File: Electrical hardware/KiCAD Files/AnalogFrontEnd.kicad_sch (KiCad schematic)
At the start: 0 parts

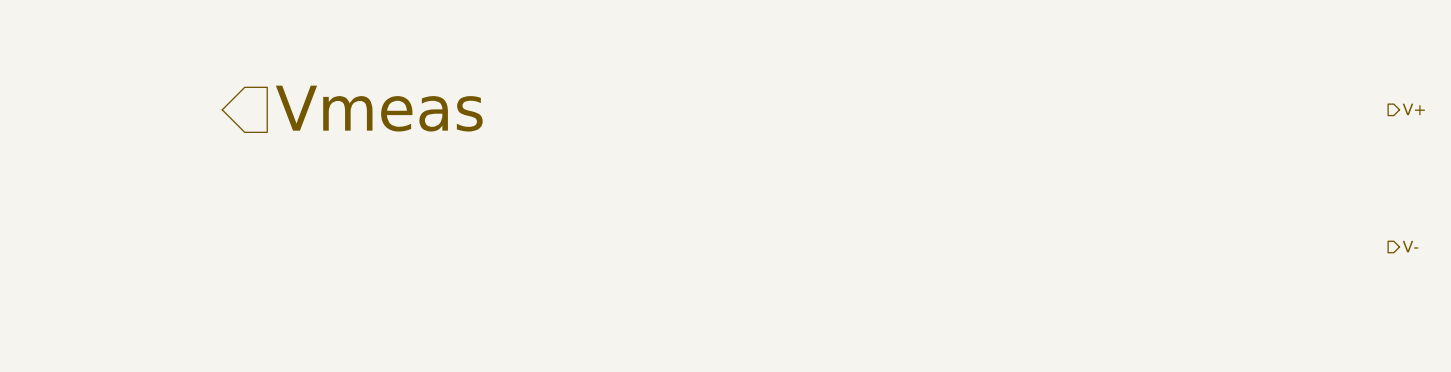
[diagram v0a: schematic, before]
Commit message: adding voltage divider
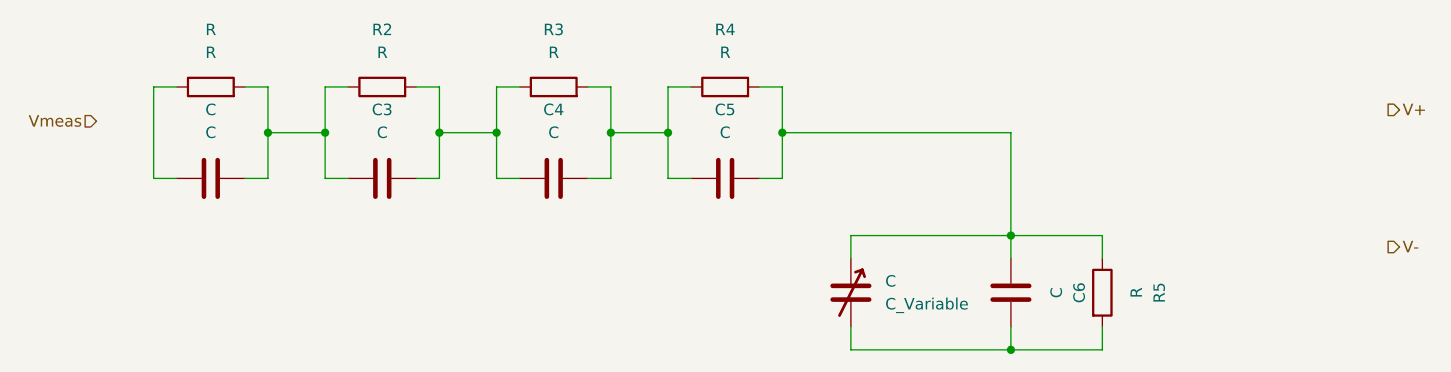
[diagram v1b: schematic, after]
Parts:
- added C: C_Variable, symbol Device:C_Variable
- added C, C3, C4, C5, C6: C, symbol Device:C
- added R, R2, R3, R4, R5: R, symbol Device:R
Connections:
- new net: C4.2, C5.1, R3.2, R4.1
- new net: C.1, C5.2, C6.1, R4.2, R5.1
- new net: C.2, C6.2, R5.2
- new net: C3.2, C4.1, R2.2, R3.1
- new net: C.1, R.1
- new net: C.2, C3.1, R.2, R2.1
